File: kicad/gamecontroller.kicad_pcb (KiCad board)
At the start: 4 copper layers, 114.7 x 54.7 mm, 19 parts, among them SW1 SW_Push, SW2 SW_Push, SW3 SW_Push, SW4 SW_Push, SW5 SW_Push, SW6 SW_Push

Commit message: Updates to kicad files and update espinput submodule
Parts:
- added D1: LED, LED_THT:LED_D3.0mm, F.Cu at (184.9, 54.1)
- U1: value ~ -> ESP32_30pin
- moved U1 0.74 mm to (164.4, 78.3)
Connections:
- C1 pad 2: Net-(U1-GPIO13) -> Net-(C1-Pad2)
- C2 pad 2: Net-(U1-GPIO14) -> Net-(C2-Pad2)
- C3 pad 2: Net-(U1-GPIO27) -> Net-(C3-Pad2)
- C5 pad 2: Net-(U1-GPIO19) -> Net-(C5-Pad2)
- C6 pad 2: Net-(U1-GPIO18) -> Net-(C6-Pad2)
- R1 pad 2: Net-(U1-GPIO13) -> Net-(C1-Pad2)
- R2 pad 2: Net-(U1-GPIO14) -> Net-(C2-Pad2)
- R3 pad 2: Net-(U1-GPIO27) -> Net-(C3-Pad2)
- R5 pad 2: Net-(U1-GPIO19) -> Net-(C5-Pad2)
- R6 pad 2: Net-(U1-GPIO18) -> Net-(C6-Pad2)
- SW1 pad 2: Net-(U1-GPIO13) -> Net-(C1-Pad2)
- SW2 pad 2: Net-(U1-GPIO14) -> Net-(C2-Pad2)
- SW3 pad 2: Net-(U1-GPIO27) -> Net-(C3-Pad2)
- SW5 pad 2: Net-(U1-GPIO19) -> Net-(C5-Pad2)
- SW6 pad 2: Net-(U1-GPIO18) -> Net-(C6-Pad2)
- U1 pad 24: Net-(U1-GPIO18) -> unconnected-(U1-GPIO18-Pad24)
- U1 pad 25: Net-(U1-GPIO19) -> unconnected-(U1-GPIO19-Pad25)
- U1 pad 3: Net-(U1-GPIO13) -> unconnected-(U1-GPIO13-Pad3)
- U1 pad 5: Net-(U1-GPIO14) -> unconnected-(U1-GPIO14-Pad5)
- U1 pad 6: Net-(U1-GPIO27) -> unconnected-(U1-GPIO27-Pad6)
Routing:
- net Net-(U1-GPIO14): track 26.5 -> 0.00 mm
- net Net-(C2-Pad2): track 0.00 -> 26.5 mm
- net Net-(U1-GPIO13): track 22.5 -> 0.00 mm
- net Net-(C1-Pad2): track 0.00 -> 22.5 mm
- net Net-(U1-GPIO19): track 5.13 -> 0.00 mm
- net Net-(C5-Pad2): track 0.00 -> 5.13 mm
- net Net-(U1-GPIO27): track 5.11 -> 0.00 mm
- net Net-(C3-Pad2): track 0.00 -> 5.11 mm
- net Net-(U1-GPIO18): track 5.03 -> 0.00 mm
- net Net-(C6-Pad2): track 0.00 -> 5.03 mm

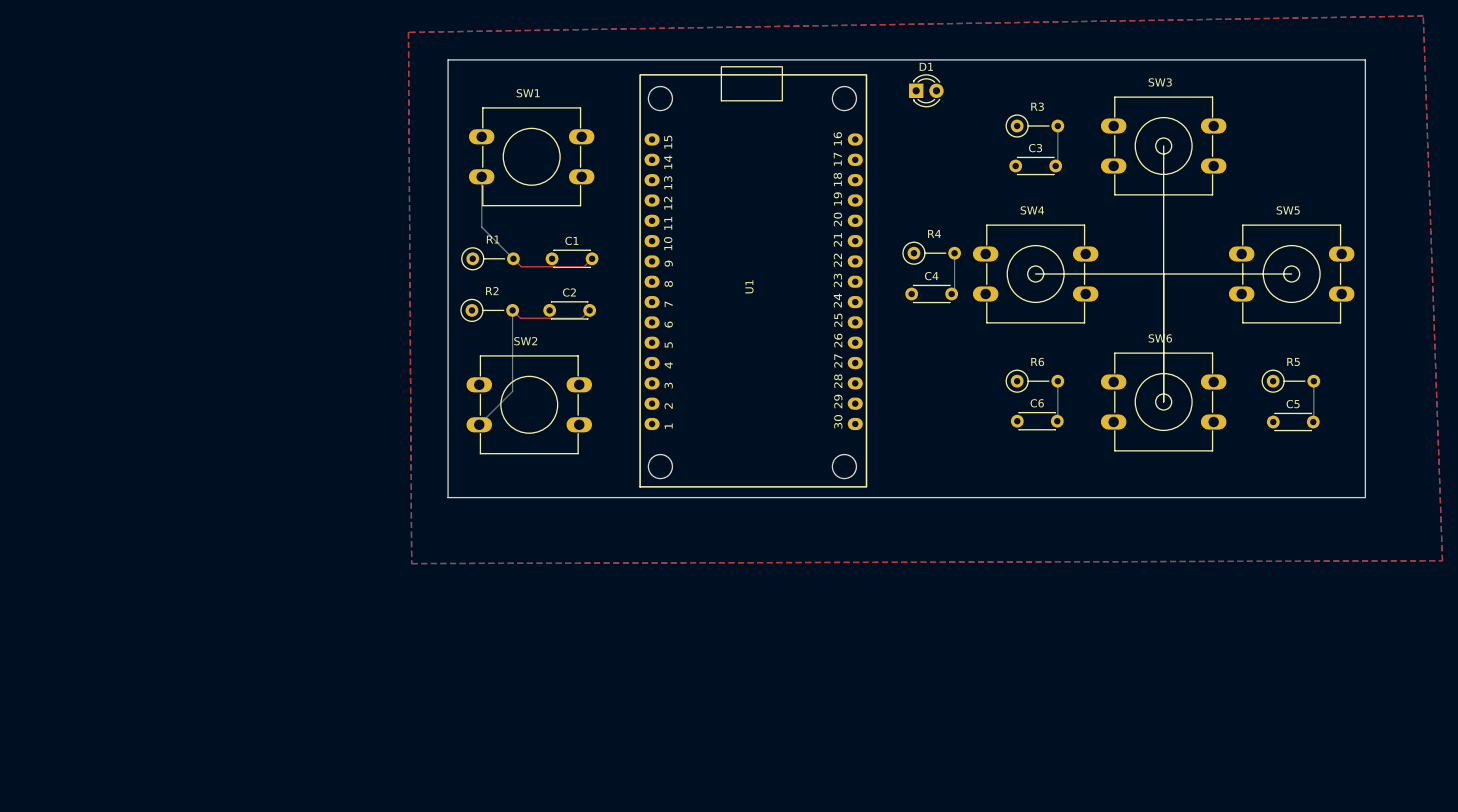
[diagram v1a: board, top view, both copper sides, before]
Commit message: Update kicad, gerber, and spice files
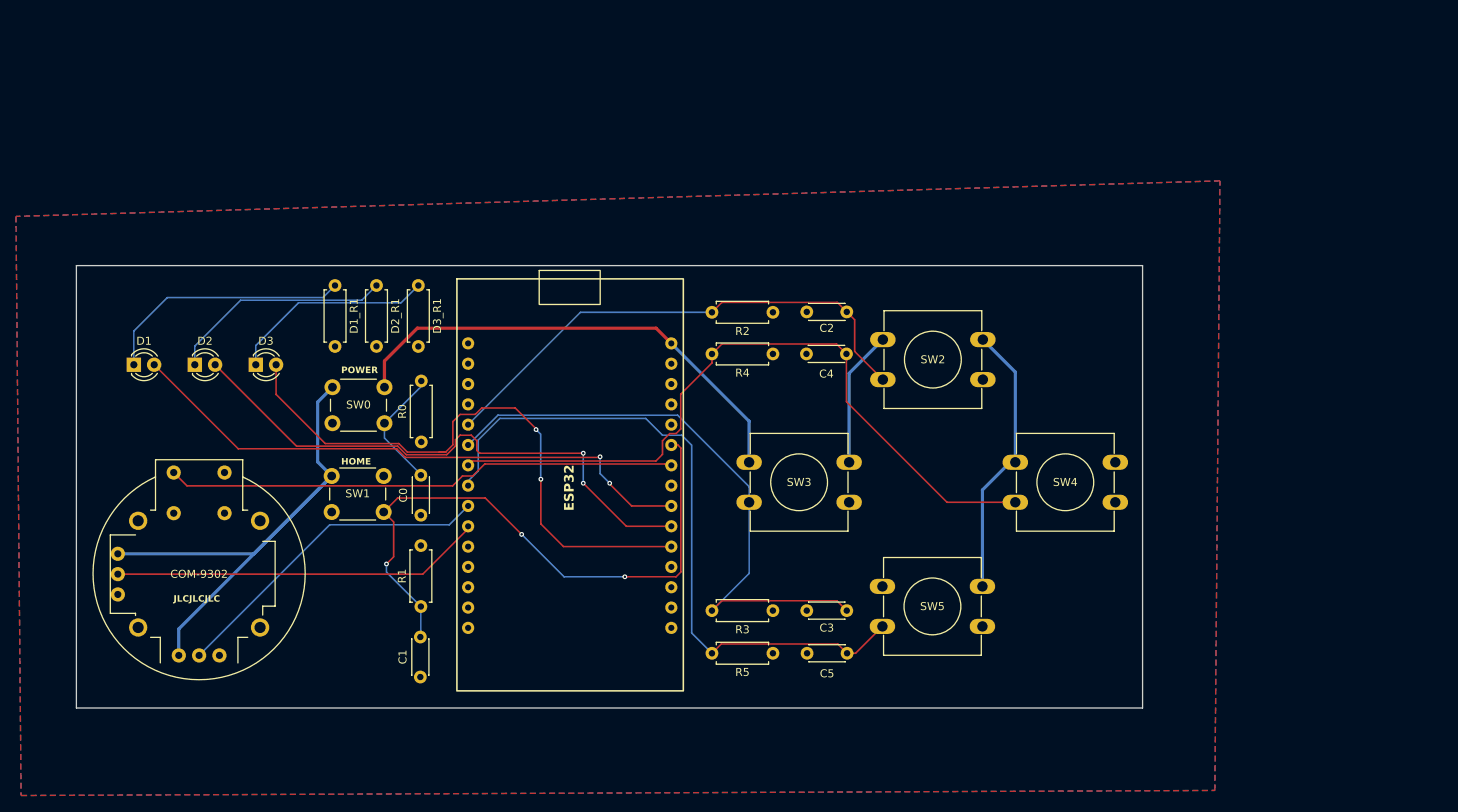
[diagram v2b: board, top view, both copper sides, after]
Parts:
- removed C6: 100nF, Capacitor_THT:C_Disc_D4.3mm_W1.9mm_P5.00mm
- removed R6: 10K, Resistor_THT:R_Axial_DIN0207_L6.3mm_D2.5mm_P5.08mm_Vertical
- removed SW6: SW_Push, Button_Switch_THT:SW_PUSH-12mm
- removed U1: ESP32_30pin, ESP32_30pin:ESP32_30pin
- added C0: 100nF, Capacitor_THT:C_Disc_D4.3mm_W1.9mm_P5.00mm, F.Cu at (123.0, 107.2)
- added COM-9302: COM-09032, COM_09302:XDCR_COM-09032, F.Cu at (95.3, 114.6)
- added D1_R1: 330, Resistor_THT:R_Axial_DIN0207_L6.3mm_D2.5mm_P7.62mm_Horizontal, F.Cu at (112.3, 78.5)
- added D2: LED, LED_THT:LED_D3.0mm, F.Cu at (94.7, 88.4)
- added D2_R1: 330, Resistor_THT:R_Axial_DIN0207_L6.3mm_D2.5mm_P7.62mm_Horizontal, F.Cu at (117.5, 78.5)
- added D3: LED, LED_THT:LED_D3.0mm, F.Cu at (102.4, 88.4)
- added D3_R1: 330, Resistor_THT:R_Axial_DIN0207_L6.3mm_D2.5mm_P7.62mm_Horizontal, F.Cu at (122.7, 78.5)
- added ESP32: ESP32_30pin, ESP32:ESP32_connector_30pin, F.Cu at (141.6, 103.5)
- added R0: 10K, Resistor_THT:R_Axial_DIN0207_L6.3mm_D2.5mm_P7.62mm_Horizontal, F.Cu at (123.0, 98.0)
- added SW0: SW_Push, Button_Switch_THT:SW_PUSH_6mm, F.Cu at (112.0, 91.2)
- R1, R2, R3, R4, R5: footprint Resistor_THT:R_Axial_DIN0207_L6.3mm_D2.5mm_P5.08mm_Vertical -> Resistor_THT:R_Axial_DIN0207_L6.3mm_D2.5mm_P7.62mm_Horizontal
- SW1: footprint Button_Switch_THT:SW_PUSH-12mm -> Button_Switch_THT:SW_PUSH_6mm
- moved D1 103.6 mm to (87.1, 88.4)
- moved R5 71.2 mm to (167.0, 124.5), turned to 180 degrees
- moved R3 67.8 mm to (167.0, 119.1), turned to 180 degrees
- moved C5 65.1 mm to (171.3, 124.5)
- moved SW3 62.0 mm to (164.0, 100.6)
- moved C3 61.4 mm to (171.2, 119.1)
- moved SW5 61.2 mm to (180.7, 116.1)
- moved C1 54.8 mm to (122.9, 127.4), turned to 90 degrees
- moved SW2 50.8 mm to (180.8, 85.2)
- moved SW1 46.4 mm to (111.8, 102.3)
- moved R2 37.6 mm to (167.0, 81.8), turned to 180 degrees
- moved R1 36.4 mm to (123.0, 111.0), turned to -90 degrees
- moved C2 32.1 mm to (171.2, 81.8)
- moved SW4 26.3 mm to (197.3, 100.6)
- moved R4 21.7 mm to (167.0, 87.0), turned to 180 degrees
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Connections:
- D1 pad 1: unconnected-(D1-K-Pad1) -> Net-(D1-K)
- D1 pad 2: unconnected-(D1-A-Pad2) -> Net-(D1-A)
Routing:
- net +3.3V: track 0.00 -> 185.9 mm
- net Net-(ESP32-GPIO26): track 5.25 -> 90.6 mm
- net Net-(ESP32-GPIO25): track 5.13 -> 86.1 mm
- net Net-(D3-A): track 0.00 -> 74.7 mm, vias 0 -> 2
- net Net-(D1-A): track 0.00 -> 73.3 mm, vias 0 -> 2
- net Net-(D2-A): track 0.00 -> 70.8 mm, vias 0 -> 2
- net Net-(ESP32-GPIO27): track 5.11 -> 75.7 mm
- net Net-(COM-9302-SEL+): track 0.00 -> 64.1 mm
- net Net-(ESP32-GPIO16): track 22.5 -> 77.5 mm, vias 0 -> 3
- net Net-(COM-9302-V): track 0.00 -> 46.4 mm
- net Net-(COM-9302-H): track 0.00 -> 41.4 mm
- net Net-(ESP32-GPIO14): track 26.5 -> 64.5 mm
- net Net-(D1-K): track 0.00 -> 31.7 mm
- net Net-(D2-K): track 0.00 -> 28.2 mm
- net Net-(D3-K): track 0.00 -> 25.8 mm
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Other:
- board size 114.7 x 54.7 mm -> 133.3 x 55.3 mm
- board text added: "HOME"
- board text added: "JLCJLCJLC"
- board text added: "POWER"
